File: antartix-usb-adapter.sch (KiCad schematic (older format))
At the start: 113 parts, among them IC1 FT2232D, J1 QTE-020-04-L-D-A, J2 0022232041, J3 614004185023, J4 WE_629105150521, J5 614004185023, J6 614004185023, U1 PCT2075GVX, U2 PAC1934T-I_JQ, U3 USB2514B-I_M2, U4 TPS2024DR, U5 TPS2024DR, U6 TPS2024DR, Y1 7C-24.000MBB-T, Y2 MQ-6.000-12-30_30_

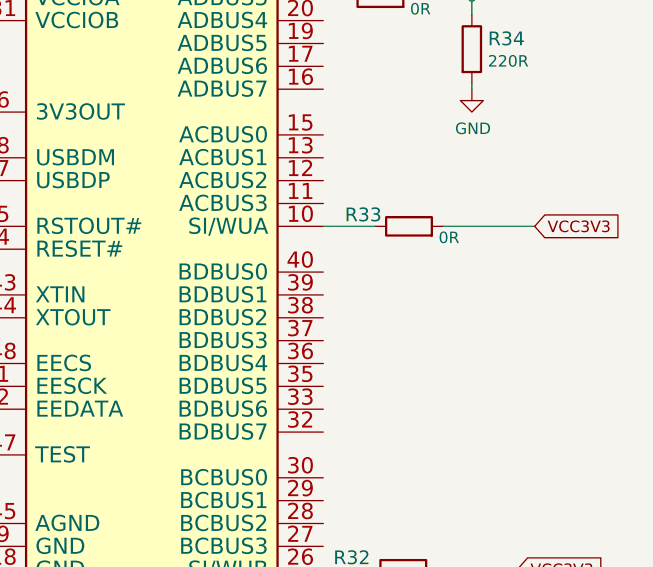
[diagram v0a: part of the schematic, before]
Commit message: Connect UART(GPIO14 & GPIO15)to BDBUS of FTDI
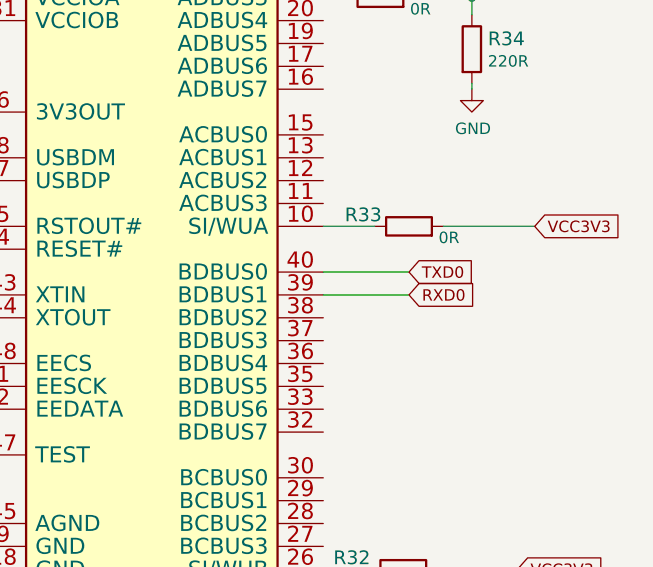
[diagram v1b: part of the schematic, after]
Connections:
- net RXD0: now reaches IC1.39 (BDBUS1)
- net TXD0: now reaches IC1.40 (BDBUS0)
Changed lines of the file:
@@
 	1    0    0    -1
 $EndComp
+Text GLabel 15100 7850 2    50   Input ~ 0
+TXD0
+Text GLabel 15100 7950 2    50   Input ~ 0
+RXD0
+Wire Wire Line
+	15100 7850 14725 7850
+Wire Wire Line
+	15100 7950 14725 7950
 $EndSCHEMATC
